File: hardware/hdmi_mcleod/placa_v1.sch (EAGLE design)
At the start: 4 parts, among them J10 M14, J11 M14, J9 M14

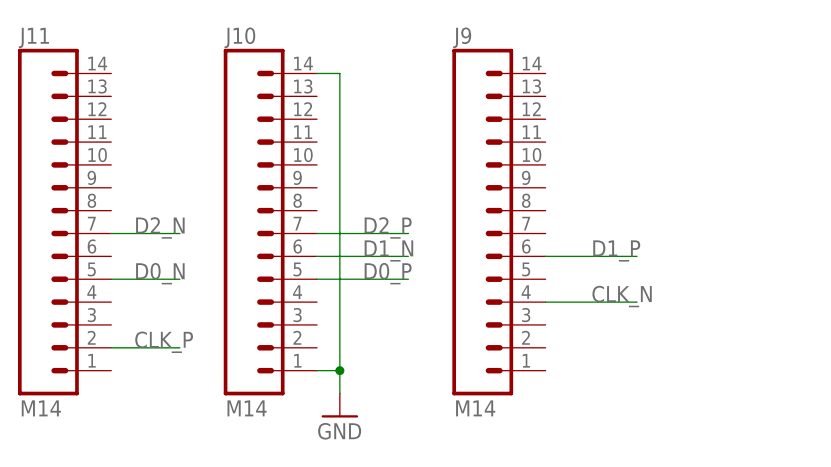
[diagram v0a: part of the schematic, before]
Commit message: 
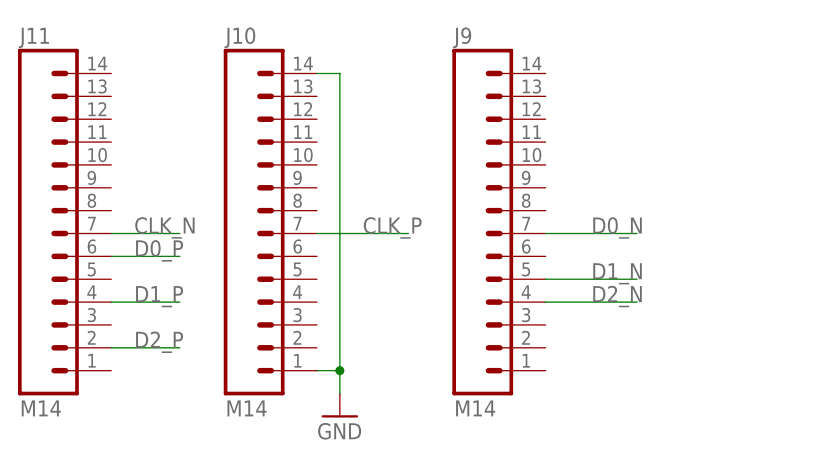
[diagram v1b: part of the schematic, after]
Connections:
- net CLK_N: now also J11.7; no longer J9.4
- net CLK_P: now also J10.7; no longer J11.2
- net D0_N: now also J9.7; no longer J11.5
- net D0_P: now also J11.6; no longer J10.5
- net D1_N: now also J9.5; no longer J10.6
- net D1_P: now also J11.4; no longer J9.6
- net D2_N: now also J9.4; no longer J11.7
- net D2_P: now also J11.2; no longer J10.7
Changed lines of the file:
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@@
 </segment>
 <segment>
-<pinref part="J10" gate="G$1" pin="7"/>
-<wire x1="35.56" y1="27.94" x2="45.72" y2="27.94" width="0.1524" layer="91"/>
-<label x="40.64" y="27.94" size="1.778" layer="95"/>
+<pinref part="J11" gate="G$1" pin="2"/>
+<wire x1="12.7" y1="15.24" x2="20.32" y2="15.24" width="0.1524" layer="91"/>
+<label x="15.24" y="15.24" size="1.778" layer="95"/>
 </segment>
 </net>
@@
 </segment>
 <segment>
-<pinref part="J11" gate="G$1" pin="7"/>
-<wire x1="12.7" y1="27.94" x2="20.32" y2="27.94" width="0.1524" layer="91"/>
-<label x="15.24" y="27.94" size="1.778" layer="95"/>
+<pinref part="J9" gate="G$1" pin="4"/>
+<wire x1="60.96" y1="20.32" x2="71.12" y2="20.32" width="0.1524" layer="91"/>
+<label x="66.04" y="20.32" size="1.778" layer="95"/>
 </segment>
 </net>
@@
 </segment>
 <segment>
-<pinref part="J9" gate="G$1" pin="6"/>
-<wire x1="60.96" y1="25.4" x2="71.12" y2="25.4" width="0.1524" layer="91"/>
-<label x="66.04" y="25.4" size="1.778" layer="95"/>
+<pinref part="J11" gate="G$1" pin="4"/>
+<wire x1="12.7" y1="20.32" x2="20.32" y2="20.32" width="0.1524" layer="91"/>
+<label x="15.24" y="20.32" size="1.778" layer="95"/>
 </segment>
 </net>
@@
 </segment>
 <segment>
-<pinref part="J10" gate="G$1" pin="6"/>
-<wire x1="35.56" y1="25.4" x2="45.72" y2="25.4" width="0.1524" layer="91"/>
-<label x="40.64" y="25.4" size="1.778" layer="95"/>
+<pinref part="J9" gate="G$1" pin="5"/>
+<wire x1="60.96" y1="22.86" x2="71.12" y2="22.86" width="0.1524" layer="91"/>
+<label x="66.04" y="22.86" size="1.778" layer="95"/>
 </segment>
 </net>
@@
 </segment>
 <segment>
-<pinref part="J10" gate="G$1" pin="5"/>
-<wire x1="35.56" y1="22.86" x2="45.72" y2="22.86" width="0.1524" layer="91"/>
-<label x="40.64" y="22.86" size="1.778" layer="95"/>
+<pinref part="J11" gate="G$1" pin="6"/>
+<wire x1="12.7" y1="25.4" x2="20.32" y2="25.4" width="0.1524" layer="91"/>
+<label x="15.24" y="25.4" size="1.778" layer="95"/>
 </segment>
 </net>
@@
 </segment>
 <segment>
-<pinref part="J11" gate="G$1" pin="5"/>
-<wire x1="12.7" y1="22.86" x2="20.32" y2="22.86" width="0.1524" layer="91"/>
-<label x="15.24" y="22.86" size="1.778" layer="95"/>
+<pinref part="J9" gate="G$1" pin="7"/>
+<wire x1="60.96" y1="27.94" x2="71.12" y2="27.94" width="0.1524" layer="91"/>
+<label x="66.04" y="27.94" size="1.778" layer="95"/>
 </segment>
 </net>
@@
 </segment>
 <segment>
-<pinref part="J11" gate="G$1" pin="2"/>
-<wire x1="12.7" y1="15.24" x2="20.32" y2="15.24" width="0.1524" layer="91"/>
-<label x="15.24" y="15.24" size="1.778" layer="95"/>
+<pinref part="J10" gate="G$1" pin="7"/>
+<wire x1="35.56" y1="27.94" x2="45.72" y2="27.94" width="0.1524" layer="91"/>
+<label x="40.64" y="27.94" size="1.778" layer="95"/>
 </segment>
 </net>
@@
 </segment>
 <segment>
-<pinref part="J9" gate="G$1" pin="4"/>
-<wire x1="60.96" y1="20.32" x2="71.12" y2="20.32" width="0.1524" layer="91"/>
-<label x="66.04" y="20.32" size="1.778" layer="95"/>
+<pinref part="J11" gate="G$1" pin="7"/>
+<wire x1="12.7" y1="27.94" x2="20.32" y2="27.94" width="0.1524" layer="91"/>
+<label x="15.24" y="27.94" size="1.778" layer="95"/>
 </segment>
 </net>
